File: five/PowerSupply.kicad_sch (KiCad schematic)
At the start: 8 parts, among them U501 TPSM33625

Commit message: Update Library
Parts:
- C501: footprint Capacitor_SMD:C_1210_3225Metric -> V2_Capacitor_SMD:C_1210; symbol Device:C_Small -> V2_Capacitor:1210_10u; Manufacturer (none) -> TDK; Mouser (none) -> 810-CNA6P1X7R1H106K2; Product (none) -> CNA6P1X7R1H106K250AE; Rating (none) -> 50V
- C502: footprint Capacitor_SMD:C_0603_1608Metric -> V2_Capacitor_SMD:C_0603; symbol Device:C_Small -> V2_Capacitor:0603_0u1; Manufacturer (none) -> TDK; Mouser (none) -> 810-CGA3E2X7R1H104MA; Product (none) -> CGA3E2X7R1H104M080AA; Rating (none) -> 50V
- C503, C505: value 22u -> 10u; footprint Capacitor_SMD:C_1210_3225Metric -> V2_Capacitor_SMD:C_1210; symbol Device:C_Small -> V2_Capacitor:1210_22u; Manufacturer (none) -> TDK; Mouser (none) -> 810-CGA6P3X7R1E226M5; Product (none) -> CGA6P3X7R1E226M250AE; Rating (none) -> 25V
- C504: footprint Capacitor_SMD:C_0603_1608Metric -> V2_Capacitor_SMD:C_0603; symbol Device:C_Small -> V2_Capacitor:0603_1u; Manufacturer (none) -> TDK; Mouser (none) -> 810-CGA3E3X7R1H105K0; Product (none) -> CGA3E3X7R1H105K080AB; Rating (none) -> 50V
- R501: footprint Resistor_SMD:R_0603_1608Metric -> V2_Resistor_SMD:R_0603; symbol Device:R_Small -> V2_Resistor:0603_27k
- R502: footprint Resistor_SMD:R_0603_1608Metric -> V2_Resistor_SMD:R_0603; symbol Device:R_Small -> V2_Resistor:0603_10k; Manufacturer (none) -> Vishay; Mouser (none) -> 71-CRCW060310K0FKEAC; Product (none) -> CRCW060310K0FKEAC; Rating (none) -> 100mW
- U501: footprint V2_Converter_DCDC:TPSM33625 -> V2_Converter_DCDC:QFN-11; symbol V2_Converter_DCDC:TPSM33625 -> V2_Converter_DCDC:TPSM33625RDNR; Manufacturer (none) -> Texas Instruments; Mouser (none) -> 595-TPSM33625RDNR; Product (none) -> TPSM33625RDNR; Rating (none) -> 2.5A

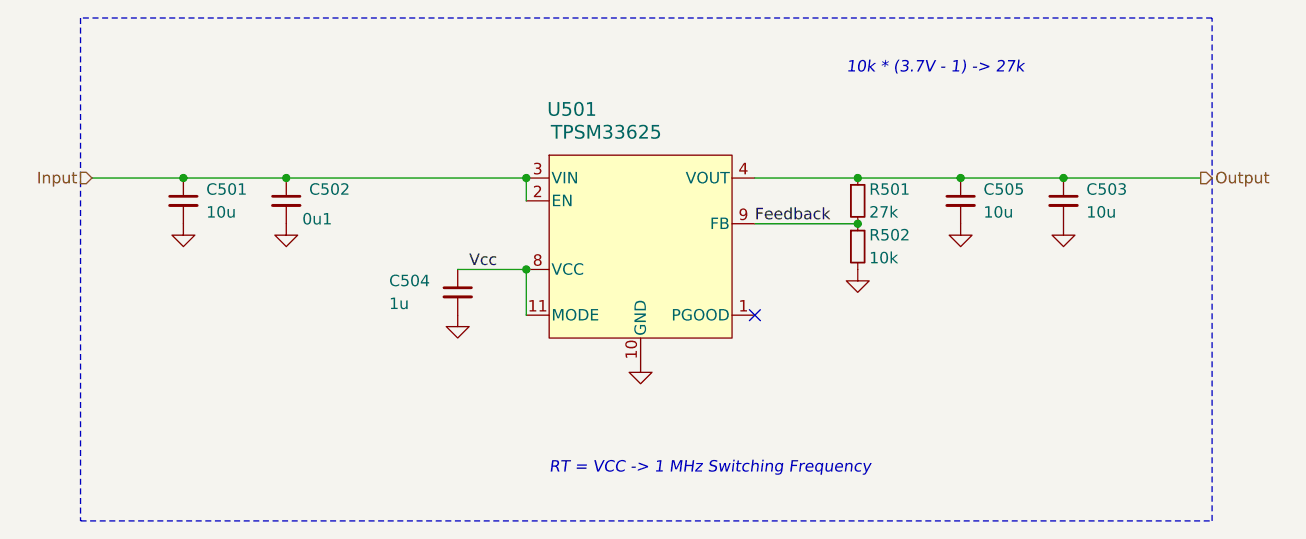
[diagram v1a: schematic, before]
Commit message: KiCad 10
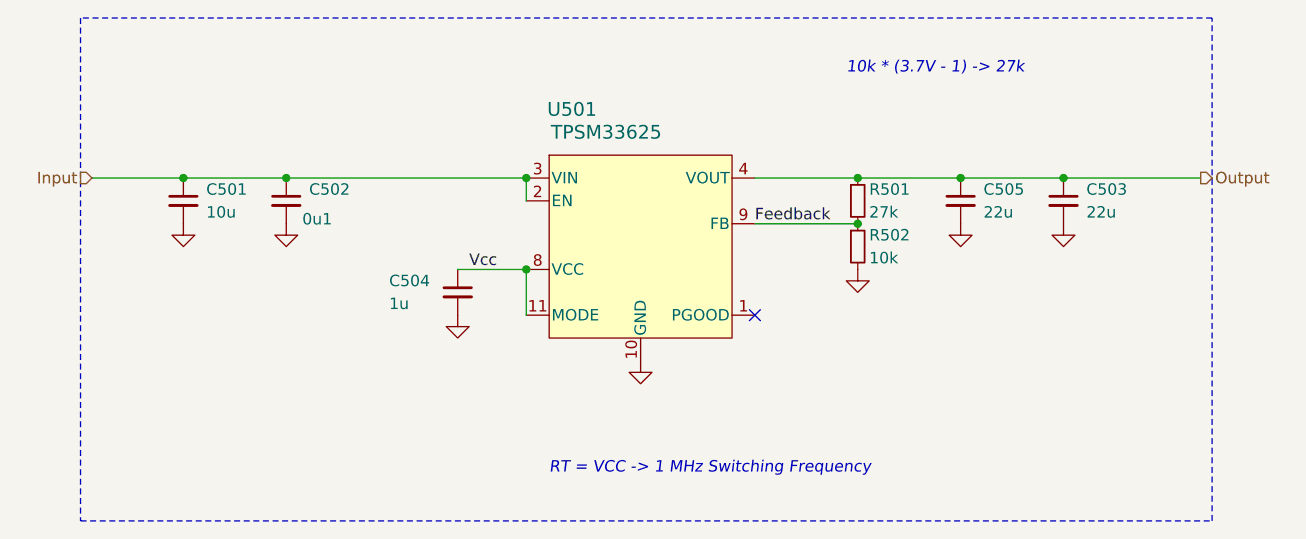
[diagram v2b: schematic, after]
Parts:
- C503, C505: value 10u -> 22u
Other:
- title: Power Supply -> Raspberry Pi 5

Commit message: Replace step-down
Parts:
- C501: Mouser 810-CNA6P1X7R1H106K2 -> 810-CNC6P1X7R1H106K2; Product CNA6P1X7R1H106K250AE -> CNC6P1X7R1H106K250AE
- U501: value TPSM33625 -> TPSM33620S5QRDNRQ1; symbol V2_Converter_DCDC:TPSM33625RDNR -> V2_Converter_DCDC:TPSM33620S5QRDNRQ1; Mouser 595-TPSM33625RDNR -> 595-SM33620S5QRDNRQ1; Product TPSM33625RDNR -> TPSM33620S5QRDNRQ1; Rating 2.5A -> 2A
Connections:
- net GND: now also U501.11 (MODE)
- net Vcc: no longer U501.11 (MODE)
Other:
- note removed: "RT = VCC -> 1 MHz Switching Frequency"
- moved on the sheet: C504
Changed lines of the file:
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@@
 	(title_block
 		(title "Raspberry Pi 5")
-		(date "2026-02-15")
-		(rev "2026-02-15")
+		(date "2026-03-31")
+		(rev "2026-03-31")
 		(company "+3V7")
 	)
@@
 		)
 	)
-	(text "RT = VCC -> 1 MHz Switching Frequency"
-		(exclude_from_sim no)
-		(at 140.97 127 0)
-		(effects
-			(font
-				(size 1.27 1.27)
-				(italic yes)
-			)
-			(justify left bottom)
-		)
-	)
 	(junction
 		(at 111.76 93.98)
@@
 	)
 	(junction
-		(at 138.43 104.14)
-		(diameter 0)
-		(color 0 0 0 0)
-	)
-	(junction
 		(at 175.26 93.98)
 		(diameter 0)
@@
 			(width 0)
 			(type dash)
-		)
-	)
-	(wire
-		(pts
-			(xy 138.43 104.14) (xy 138.43 109.22)
-		)
-		(stroke
-			(width 0)
-			(type default)
 		)
 	)
@@
 	(symbol
 		(lib_id "V2_power:GND")
-		(at 130.81 109.22 0)
+		(at 125.73 104.14 270)
 		(unit 1)
 		(body_style 1)
@@
 		(dnp no)
 		(property "Reference" "#PWR506"
-			(at 130.81 115.57 0)
+			(at 119.38 104.14 0)
 			(hide yes)
 			(show_name no)
@@
 		)
 		(property "Value" "GND"
-			(at 130.81 114.3 0)
+			(at 120.65 104.14 0)
 			(hide yes)
 			(show_name no)
@@
 		)
 		(property "Footprint" ""
-			(at 130.81 109.22 0)
+			(at 125.73 104.14 0)
 			(hide yes)
 			(show_name no)
@@
 		)
 		(property "Datasheet" ""
-			(at 130.81 109.22 0)
+			(at 125.73 104.14 0)
 			(hide yes)
 			(show_name no)
@@
 		)
 		(property "Description" ""
-			(at 130.81 109.22 0)
+			(at 125.73 104.14 0)
 			(hide yes)
 			(show_name no)
@@
 	)
 	(symbol
-		(lib_id "V2_Converter_DCDC:TPSM33625RDNR")
+		(lib_id "V2_power:GND")
+		(at 138.43 109.22 270)
+		(unit 1)
+		(body_style 1)
+		(exclude_from_sim no)
+		(in_bom yes)
+		(on_board yes)
+		(in_pos_files yes)
+		(dnp no)
+		(property "Reference" "#PWR509"
+			(at 132.08 109.22 0)
+			(hide yes)
+			(show_name no)
+			(do_not_autoplace no)
+			(effects
+				(font
+					(size 1.27 1.27)
+				)
+			)
+		)
+		(property "Value" "GND"
+			(at 133.35 109.22 0)
+			(hide yes)
+			(show_name no)
+			(do_not_autoplace no)
+			(effects
+				(font
+					(size 1.27 1.27)
+				)
+			)
+		)
+		(property "Footprint" ""
+			(at 138.43 109.22 0)
+			(hide yes)
+			(show_name no)
+			(do_not_autoplace no)
+			(effects
+				(font
+					(size 1.27 1.27)
+				)
+			)
+		)
+		(property "Datasheet" ""
+			(at 138.43 109.22 0)
+			(hide yes)
+			(show_name no)
+			(do_not_autoplace no)
+			(effects
+				(font
+					(size 1.27 1.27)
+				)
+			)
+		)
+		(property "Description" ""
+			(at 138.43 109.22 0)
+			(hide yes)
+			(show_name no)
+			(do_not_autoplace no)
+			(effects
+				(font
+					(size 1.27 1.27)
+				)
+			)
+		)
+		(pin "1"
+		)
+		(instances
+			(project "raspberry-pi-5"
+				(path "/6c8448b4-b04d-47e1-934e-e40cbe27a7be/1dfd0340-8008-42a6-85d2-0bfe9a8029cf"
+					(reference "#PWR509")
+					(unit 1)
+				)
+			)
+		)
+	)
+	(symbol
+		(lib_id "V2_Converter_DCDC:TPSM33620S5QRDNRQ1")
 		(at 151.13 101.6 0)
 		(unit 1)
@@
 			)
 		)
-		(property "Value" "TPSM33625"
+		(property "Value" "TPSM33620S5QRDNRQ1"
 			(at 147.32 88.9 0)
 			(show_name no)
@@
 			)
 		)
-		(property "Mouser" "595-TPSM33625RDNR"
+		(property "Mouser" "595-SM33620S5QRDNRQ1"
 			(at 151.13 149.86 0)
 			(hide yes)
@@
 			)
 		)
-		(property "Product" "TPSM33625RDNR"
+		(property "Product" "TPSM33620S5QRDNRQ1"
 			(at 151.13 147.32 0)
 			(hide yes)
@@
 			)
 		)
-		(property "Rating" "2.5A"
+		(property "Rating" "2A"
 			(at 151.13 152.4 0)
 			(hide yes)
@@
 			)
 		)
-		(property "Mouser" "810-CNA6P1X7R1H106K2"
+		(property "Mouser" "810-CNC6P1X7R1H106K2"
 			(at 100.33 119.38 0)
 			(hide yes)
@@
 			)
 		)
-		(property "Product" "CNA6P1X7R1H106K250AE"
+		(property "Product" "CNC6P1X7R1H106K250AE"
 			(at 100.33 114.3 0)
 			(hide yes)
@@
 	(symbol
 		(lib_id "V2_Capacitor:0603_1u")
-		(at 130.81 106.68 0)
+		(at 128.27 104.14 270)
 		(unit 1)
 		(body_style 1)
@@
 		(dnp no)
 		(property "Reference" "C504"
-			(at 123.19 105.41 0)
+			(at 126.492 108.204 90)
 			(show_name no)
 			(do_not_autoplace no)
@@
 		)
 		(property "Value" "1u"
-			(at 123.19 107.95 0)
+			(at 126.746 110.998 90)
 			(show_name no)
 			(do_not_autoplace no)
@@
 		)
 		(property "Footprint" "V2_Capacitor_SMD:C_0603"
-			(at 130.81 123.698 0)
+			(at 111.252 104.14 0)
 			(hide yes)
 			(show_name no)
@@
 		)
 		(property "Datasheet" ""
-			(at 130.81 106.68 0)
+			(at 128.27 104.14 0)
 			(hide yes)
 			(show_name no)
@@
 		)
 		(property "Description" ""
-			(at 130.81 119.38 0)
+			(at 115.57 104.14 0)
 			(hide yes)
 			(show_name no)
@@
 		)
 		(property "Mouser" "810-CGA3E3X7R1H105K0"
-			(at 130.81 127 0)
+			(at 107.95 104.14 0)
 			(hide yes)
 			(show_name no)
@@
 		)
 		(property "Product" "CGA3E3X7R1H105K080AB"
-			(at 130.81 124.46 0)
+			(at 110.49 104.14 0)
 			(hide yes)
 			(show_name no)
@@
 		)
 		(property "Manufacturer" "TDK"
-			(at 130.81 121.92 0)
+			(at 113.03 104.14 0)
 			(hide yes)
 			(show_name no)
@@
 		)
 		(property "Rating" "50V"
-			(at 130.81 129.54 0)
-			(hide yes)
-			(show_name no)
+			(at 105.41 104.14 0)
+			(hide yes)
+			(show_name no)

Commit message: Good Bye Imperial
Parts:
- C501: footprint V2_Capacitor_SMD:C_1210 -> V2_Capacitor_SMD:C_3225; symbol V2_Capacitor:1210_10u -> V2_Capacitor:3225_10u
- C502: footprint V2_Capacitor_SMD:C_0603 -> V2_Capacitor_SMD:C_1608; symbol V2_Capacitor:0603_0u1 -> V2_Capacitor:1608_0u1
- C503, C505: footprint V2_Capacitor_SMD:C_1210 -> V2_Capacitor_SMD:C_3225; symbol V2_Capacitor:1210_22u -> V2_Capacitor:3225_22u
- C504: footprint V2_Capacitor_SMD:C_0603 -> V2_Capacitor_SMD:C_1608; symbol V2_Capacitor:0603_1u -> V2_Capacitor:1608_1u
- R501: footprint V2_Resistor_SMD:R_0603 -> V2_Resistor_SMD:R_1608; symbol V2_Resistor:0603_27k -> V2_Resistor:1608_27k
- R502: footprint V2_Resistor_SMD:R_0603 -> V2_Resistor_SMD:R_1608; symbol V2_Resistor:0603_10k -> V2_Resistor:1608_10k
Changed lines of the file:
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@@
 	)
 	(symbol
-		(lib_id "V2_Resistor:0603_10k")
+		(lib_id "V2_Resistor:1608_10k")
 		(at 175.26 101.6 0)
 		(unit 1)
@@
 			)
 		)
-		(property "Footprint" "V2_Resistor_SMD:R_0603"
+		(property "Footprint" "V2_Resistor_SMD:R_1608"
 			(at 175.26 117.348 0)
 			(hide yes)
@@
 	)
 	(symbol
-		(lib_id "V2_Resistor:0603_27k")
+		(lib_id "V2_Resistor:1608_27k")
 		(at 175.26 96.52 0)
 		(unit 1)
@@
 			)
 		)
-		(property "Footprint" "V2_Resistor_SMD:R_0603"
+		(property "Footprint" "V2_Resistor_SMD:R_1608"
 			(at 175.26 112.268 0)
 			(hide yes)
@@
 	)
 	(symbol
-		(lib_id "V2_Capacitor:1210_10u")
+		(lib_id "V2_Capacitor:3225_10u")
 		(at 100.33 96.52 0)
 		(unit 1)
@@
 			)
 		)
-		(property "Footprint" "V2_Capacitor_SMD:C_1210"
+		(property "Footprint" "V2_Capacitor_SMD:C_3225"
 			(at 100.33 113.538 0)
 			(hide yes)
@@
 	)
 	(symbol
-		(lib_id "V2_Capacitor:0603_1u")
+		(lib_id "V2_Capacitor:1608_1u")
 		(at 128.27 104.14 270)
 		(unit 1)
@@
 			)
 		)
-		(property "Footprint" "V2_Capacitor_SMD:C_0603"
+		(property "Footprint" "V2_Capacitor_SMD:C_1608"
 			(at 111.252 104.14 0)
 			(hide yes)
@@
 	)
 	(symbol
-		(lib_id "V2_Capacitor:1210_22u")
+		(lib_id "V2_Capacitor:3225_22u")
 		(at 186.69 96.52 0)
 		(unit 1)
@@
 			)
 		)
-		(property "Footprint" "V2_Capacitor_SMD:C_1210"
+		(property "Footprint" "V2_Capacitor_SMD:C_3225"
 			(at 186.69 113.538 0)
 			(hide yes)
@@
 	)
 	(symbol
-		(lib_id "V2_Capacitor:0603_0u1")
+		(lib_id "V2_Capacitor:1608_0u1")
 		(at 111.76 96.52 0)
 		(unit 1)
@@
 			)
 		)
-		(property "Footprint" "V2_Capacitor_SMD:C_0603"
+		(property "Footprint" "V2_Capacitor_SMD:C_1608"
 			(at 111.76 113.538 0)
 			(hide yes)
@@
 	)
 	(symbol
-		(lib_id "V2_Capacitor:1210_22u")
+		(lib_id "V2_Capacitor:3225_22u")
 		(at 198.12 96.52 0)
 		(unit 1)
@@
 			)
 		)
-		(property "Footprint" "V2_Capacitor_SMD:C_1210"
+		(property "Footprint" "V2_Capacitor_SMD:C_3225"
 			(at 198.12 113.538 0)
 			(hide yes)
